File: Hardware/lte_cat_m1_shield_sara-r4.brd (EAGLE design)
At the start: 68.1 x 53.3 mm, 183 parts, among them J8 U.FL, J9 NANO_SIM, Q1 2.5A/30V/105mΩ, Q2 600mA/40V, U1 TXB0104, U2 AP2112K-3.3, U3 MCP73831, U4 TCA9406DCU, U5 AP7361C-33FGE, U6 SARA-R410M-2B

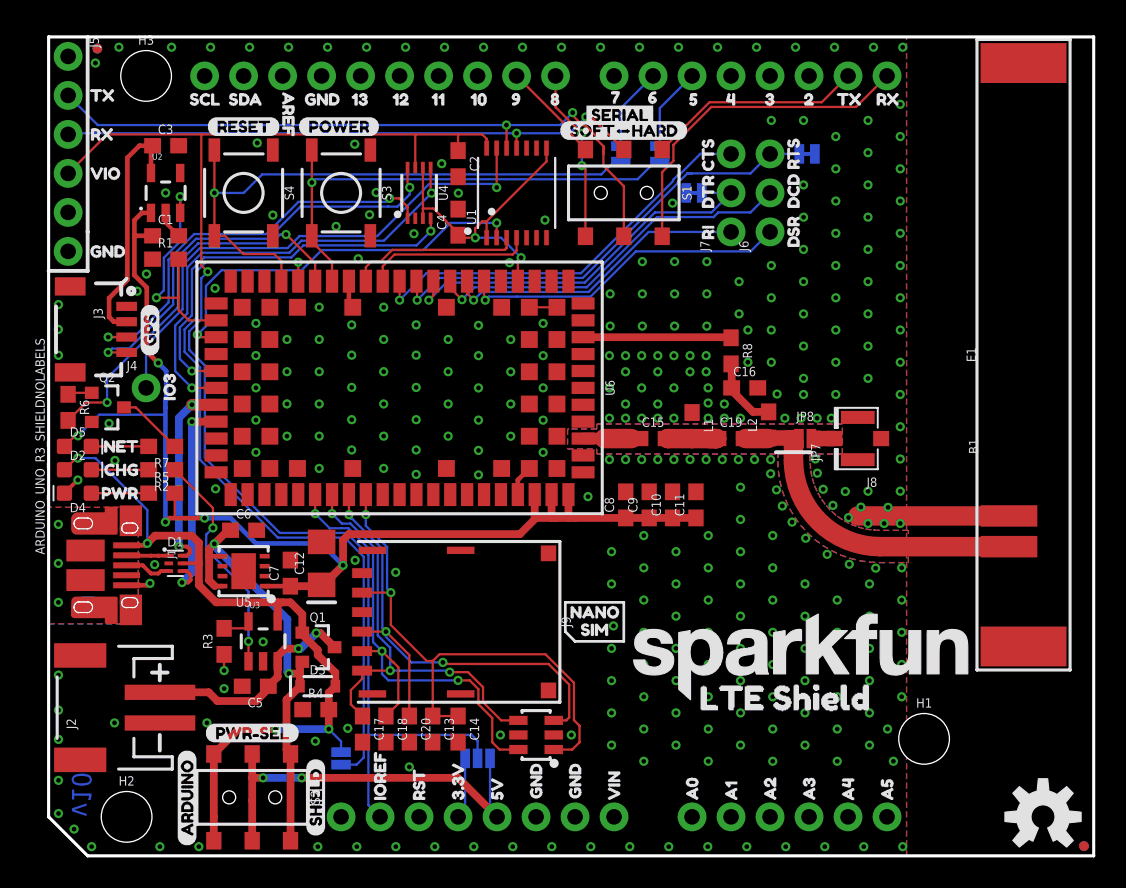
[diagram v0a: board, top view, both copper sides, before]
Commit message: Modification post-group-review. Labels, Qwiic breakouts, test points.
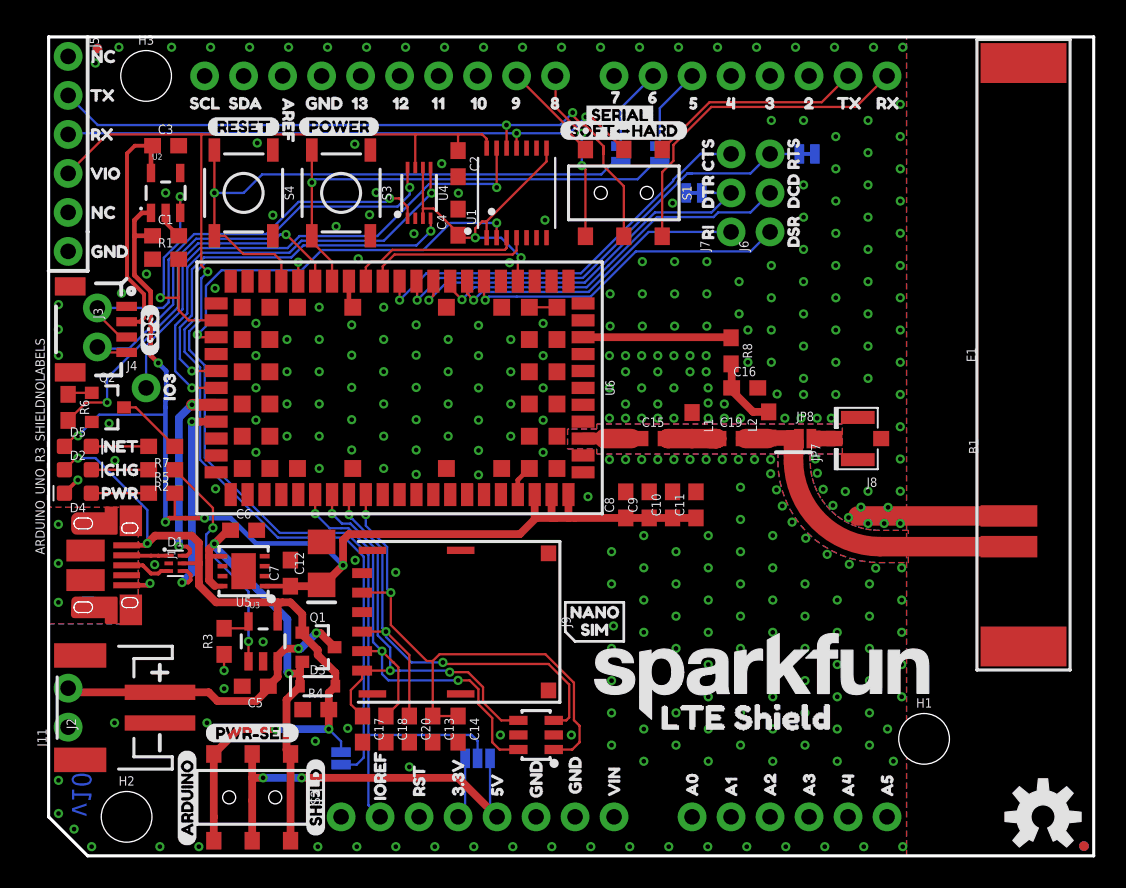
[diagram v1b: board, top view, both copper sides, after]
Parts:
- added J10, J11: (no value), SparkFun-Connectors:1X02_NO_SILK
- added U$103, U$106, U$107, U$108: (no value), buzzard_labels:NC0
- added U$109: (no value), buzzard_labels:GPS#SCL1
- added U$110: (no value), buzzard_labels:GPS#SDA0
- added U$111: (no value), buzzard_labels:VBAT2
- added U$112: (no value), buzzard_labels:GND3
- moved U$77 2.84 mm to (38.5, 9.02)
- moved LOGO1 2.84 mm to (35.6, 8.89)
- moved U$3 0.38 mm to (15.6, 50.0)
- moved U$93 0.28 mm to (34.0, 49.0)
- moved U$98 0.28 mm to (48.0, 49.0)
- moved U$1 0.25 mm to (8.51, 49.0)
- moved U$10 0.25 mm to (32.0, 49.0)
- moved U$100 0.25 mm to (53.6, 49.0)
- moved U$101 0.25 mm to (56.0, 49.0)
- moved U$15 0.25 mm to (41.0, 49.0)
- moved U$16 0.25 mm to (43.4, 49.0)
- moved U$17 0.25 mm to (45.8, 49.0)
- moved U$18 0.25 mm to (48.5, 49.0)
- moved U$2 0.25 mm to (11.0, 49.0)
- moved U$20 0.25 mm to (53.2, 49.0)
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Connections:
- net GND: now also J11.1
- net SCL-QWIIC: now also J10.2
- net SDA-QWIIC: now also J10.1
- net V_BATT: now also J11.2
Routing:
- net V_BATT: track 14.7 -> 20.8 mm
- net SDA-QWIIC: track 27.1 -> 28.7 mm, vias 2 -> 1
- net SCL-QWIIC: track 28.5 -> 30.0 mm, vias 2 -> 1
- net GND: vias 332 -> 329

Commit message: Revising product name in silk, schematic fixes.
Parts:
- C19: value 0Ohm -> 0; device SparkFun-Capacitors:0603 -> SparkFun-Resistors:0603
- U$32, U$77: device buzzard_labels:LTE_SHIELD1 -> buzzard_labels:LTE_CAT_M1#NB#IOT_SHIELD1
- moved U$54 3.30 mm to (33.4, 19.2)
- moved U$55 3.30 mm to (34.1, 18.0)
- moved U$77 2.88 mm to (36.3, 10.9)
- moved LOGO1 2.54 mm to (33.5, 10.4)
- moved U$32 0.13 mm to (40.3, 29.7)
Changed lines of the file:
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@@
 <layer number="16" name="Bottom" color="1" fill="1" visible="yes" active="yes"/>
 <layer number="17" name="Pads" color="2" fill="1" visible="yes" active="yes"/>
-<layer number="18" name="Vias" color="2" fill="1" visible="yes" active="yes"/>
+<layer number="18" name="Vias" color="2" fill="1" visible="no" active="yes"/>
 <layer number="19" name="Unrouted" color="6" fill="1" visible="yes" active="yes"/>
 <layer number="20" name="Dimension" color="15" fill="1" visible="yes" active="yes"/>
@@
 <layer number="43" name="vRestrict" color="2" fill="10" visible="no" active="yes"/>
 <layer number="44" name="Drills" color="7" fill="1" visible="no" active="yes"/>
-<layer number="45" name="Holes" color="7" fill="1" visible="no" active="yes"/>
+<layer number="45" name="Holes" color="7" fill="1" visible="yes" active="yes"/>
 <layer number="46" name="Milling" color="3" fill="1" visible="no" active="yes"/>
 <layer number="47" name="Measures" color="7" fill="1" visible="no" active="yes"/>
@@
 <layer number="50" name="dxf" color="7" fill="1" visible="no" active="yes"/>
 <layer number="51" name="tDocu" color="6" fill="1" visible="yes" active="yes"/>
-<layer number="52" name="bDocu" color="7" fill="1" visible="yes" active="yes"/>
+<layer number="52" name="bDocu" color="7" fill="1" visible="no" active="yes"/>
 <layer number="91" name="Nets" color="2" fill="1" visible="no" active="no"/>
 <layer number="92" name="Busses" color="1" fill="1" visible="no" active="no"/>
@@
 <wire x1="2.54" y1="40.64" x2="2.54" y2="53.34" width="0.254" layer="21"/>
 <wire x1="5.08" y1="37.592" x2="4.699" y2="37.211" width="0.254" layer="21"/>
-<wire x1="33.655" y1="16.51" x2="33.655" y2="14.605" width="0.1778" layer="21"/>
-<wire x1="33.655" y1="14.605" x2="34.29" y2="13.97" width="0.1778" layer="21"/>
-<wire x1="34.29" y1="13.97" x2="37.465" y2="13.97" width="0.1778" layer="21"/>
-<wire x1="37.465" y1="13.97" x2="37.465" y2="16.51" width="0.1778" layer="21"/>
-<wire x1="37.465" y1="16.51" x2="33.655" y2="16.51" width="0.1778" layer="21"/>
+<wire x1="33.782" y1="19.812" x2="33.782" y2="17.907" width="0.1778" layer="21"/>
+<wire x1="33.782" y1="17.907" x2="34.417" y2="17.272" width="0.1778" layer="21"/>
+<wire x1="34.417" y1="17.272" x2="37.592" y2="17.272" width="0.1778" layer="21"/>
+<wire x1="37.592" y1="17.272" x2="37.592" y2="19.812" width="0.1778" layer="21"/>
+<wire x1="37.592" y1="19.812" x2="33.782" y2="19.812" width="0.1778" layer="21"/>
 <wire x1="7.239" y1="12.446" x2="7.239" y2="11.43" width="0.254" layer="21"/>
 <wire x1="6.731" y1="11.938" x2="7.747" y2="11.938" width="0.254" layer="21"/>
@@
 <attribute name="PROD_ID" value="CAP-07881" x="39.37" y="27.18" size="1.778" layer="27" font="vector" ratio="15" display="off"/>
 </element>
-<element name="C19" library="SparkFun-Capacitors" package="0603" value="0Ohm" x="44.45" y="27.18">
-<attribute name="PROD_ID" value="CAP-10142" x="44.45" y="27.18" size="1.778" layer="27" font="vector" ratio="15" display="off"/>
+<element name="C19" library="SparkFun-Resistors" package="0603" value="0" x="44.45" y="27.18">
+<attribute name="PROD_ID" value="RES-08609" x="44.45" y="27.18" size="1.778" layer="27" font="vector" ratio="15" display="off"/>
 </element>
 <element name="L1" library="ublox" package="0603" value="39nH" x="41.91" y="28.026" rot="R270">
@@
 <element name="U$52" library="buzzard_labels" package="A448" value="" x="52.07" y="3.2004" rot="R90"/>
 <element name="U$53" library="buzzard_labels" package="A549" value="" x="54.61" y="3.2004" rot="R90"/>
-<element name="U$54" library="buzzard_labels" package="NANO50" value="" x="33.274" y="15.875"/>
-<element name="U$55" library="buzzard_labels" package="SIM51" value="" x="33.9598" y="14.732"/>
+<element name="U$54" library="buzzard_labels" package="NANO50" value="" x="33.401" y="19.177"/>
+<element name="U$55" library="buzzard_labels" package="SIM51" value="" x="34.0868" y="18.034"/>
 <element name="U$56" library="buzzard_labels" package="IOREF39" value="" x="30.099" y="8.001" rot="MR0"/>
 <element name="U$57" library="buzzard_labels" package="5V42" value="" x="31.75" y="6.35" rot="MR0"/>
@@
 <element name="U$40" library="buzzard_labels" package="RST0" value="" x="24.13" y="3.175" rot="R90"/>
 <element name="U$42" library="buzzard_labels" package="RST0" value="" x="24.13" y="3.175" rot="MR90"/>
-<element name="LOGO1" library="SparkFun-Aesthetics" package="SFE_LOGO_NAME_.2" value="SFE_LOGO_NAME.2_INCH" x="35.56" y="8.89"/>
-<element name="U$77" library="buzzard_labels" package="LTE_SHIELD1" value="" x="38.481" y="9.017"/>
-<element name="U$32" library="buzzard_labels" package="LTE_SHIELD1" value="" x="40.259" y="29.591" rot="MR0"/>
+<element name="LOGO1" library="SparkFun-Aesthetics" package="SFE_LOGO_NAME_.2" value="SFE_LOGO_NAME.2_INCH" x="33.528" y="10.414"/>
 <element name="LOGO3" library="SparkFun-Aesthetics" package="SFE_LOGO_NAME_.2" value="SFE_LOGO_NAME.2_INCH" x="43.18" y="29.21" rot="MR0"/>
 <element name="U$83" library="buzzard_labels" package="HTTPS###SFE#IO#T8160" value="" x="41.783" y="24.511" rot="MR0"/>
@@
 <element name="U$111" library="buzzard_labels" package="VBAT2" value="" x="6.223" y="10.922" rot="MR0"/>
 <element name="U$112" library="buzzard_labels" package="GND3" value="" x="5.715" y="8.382" rot="MR0"/>
+<element name="U$77" library="buzzard_labels" package="LTE_CAT_M1#NB#IOT_SHIELD1" value="" x="36.322" y="10.922"/>
+<element name="U$32" library="buzzard_labels" package="LTE_CAT_M1#NB#IOT_SHIELD1" value="" x="40.259" y="29.718" rot="MR0"/>
 </elements>
 <signals>

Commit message: Disconnected AREF from GND
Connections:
- net GND: no longer B1.AREF
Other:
- board text added: "v11"
- board text removed: "v10"
